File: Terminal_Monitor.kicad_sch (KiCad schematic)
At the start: 10 parts, among them J10 VoltageMonitor, J3 7460553, J4 7460553, J5 7460553, J6 7460553

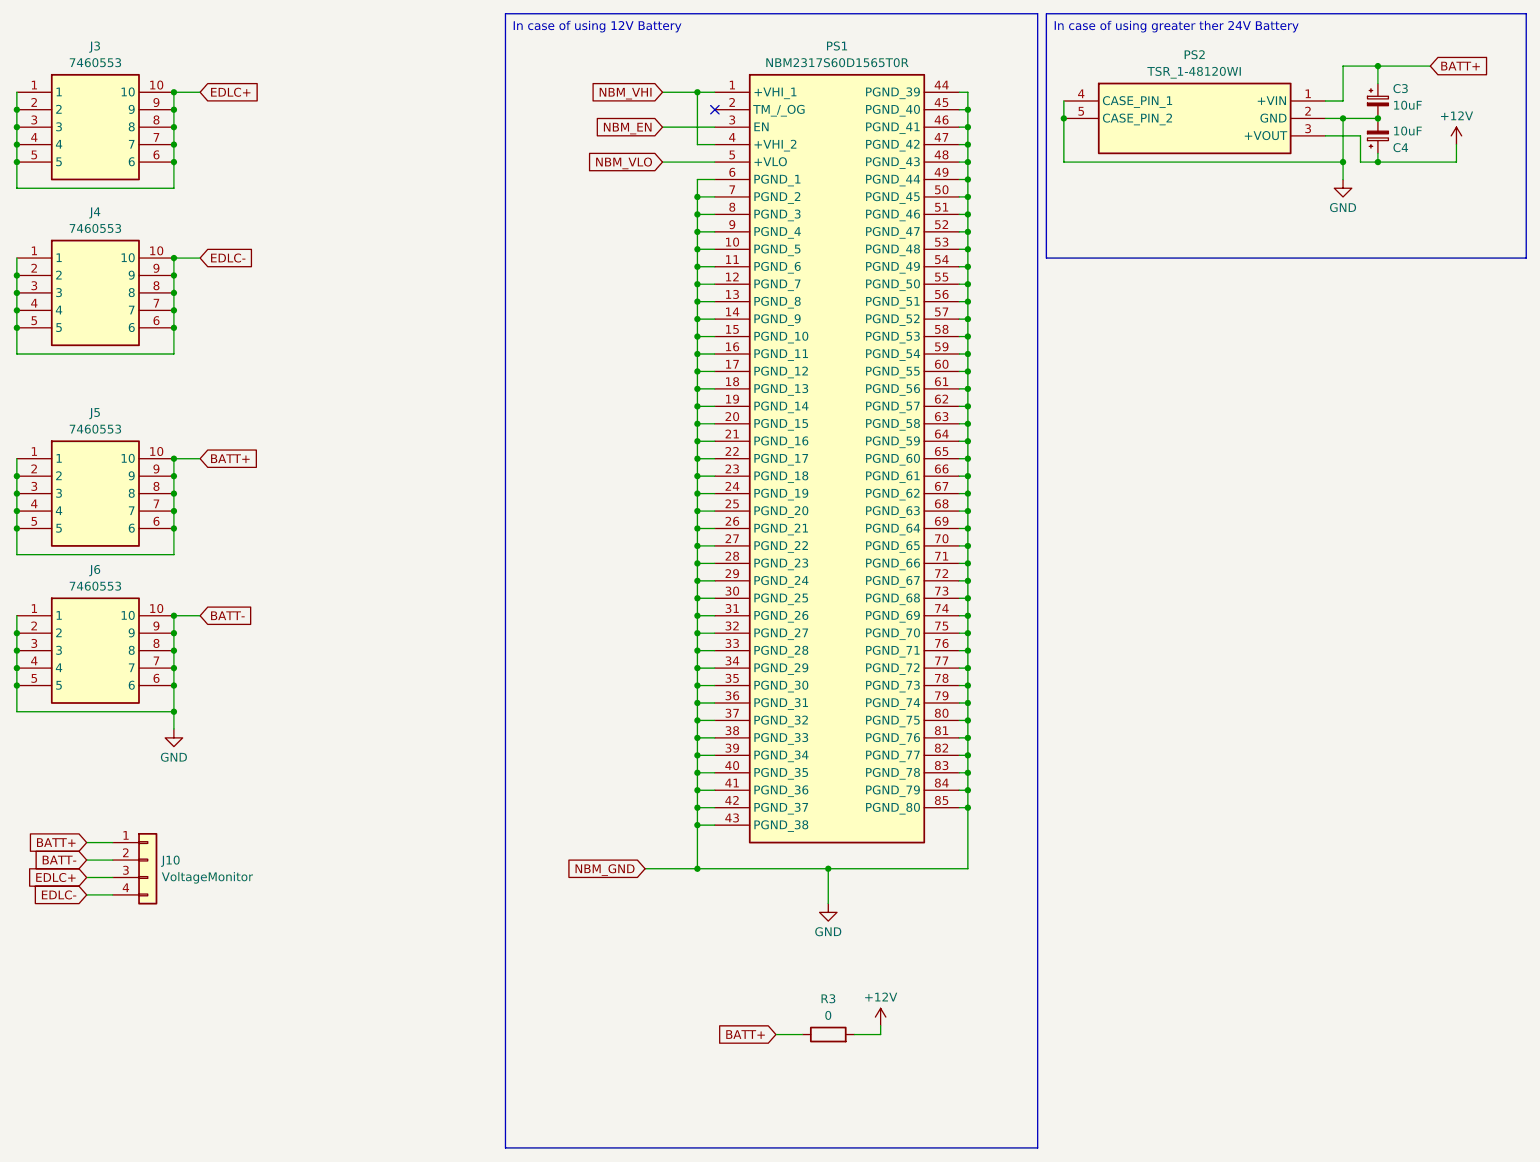
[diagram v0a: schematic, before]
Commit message: Throttle 2pin->3pin and Add C beside of NBM.
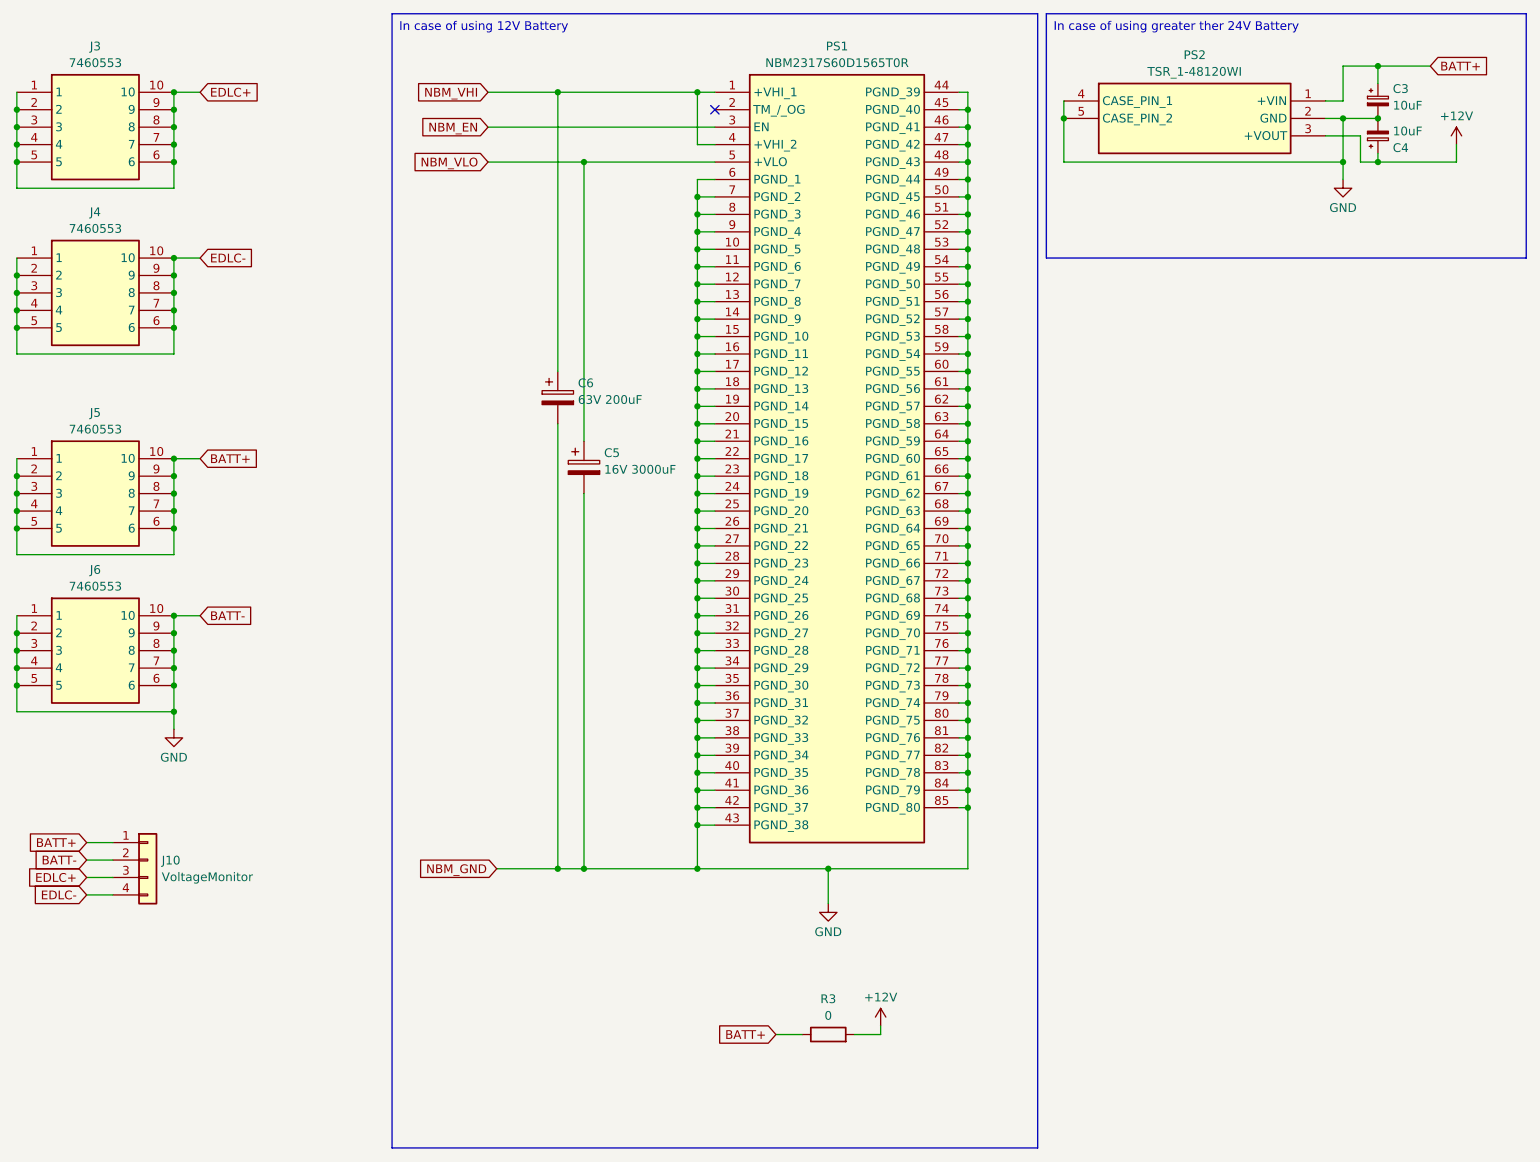
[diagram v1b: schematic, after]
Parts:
- added C5: 16V 3000uF, symbol Device:C_Polarized
- added C6: 63V 200uF, symbol Device:C_Polarized
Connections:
- net GND: now also C5.2, C6.2
- net NBM_VHI: now also C6.1
- net NBM_VLO: now also C5.1

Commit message: layout done
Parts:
- C3, C4: footprint (none) -> Capacitor_THT:CP_Radial_D5.0mm_P2.00mm
- C5: footprint (none) -> Capacitor_THT:CP_Radial_D12.5mm_P5.00mm
- C6: footprint (none) -> Capacitor_THT:CP_Radial_D10.0mm_P5.00mm
- J10: footprint (none) -> Connector_PinHeader_2.54mm:PinHeader_1x04_P2.54mm_Vertical
- J3: value 7460553 -> EDLC+; footprint 7460553 -> 7460553:7460553
- J4: value 7460553 -> EDLC-; footprint 7460553 -> 7460553:7460553
- J5: value 7460553 -> BATT+; footprint 7460553 -> 7460553:7460553
- J6: value 7460553 -> BATT-; footprint 7460553 -> 7460553:7460553
- PS1: footprint NBM2317S60D1565T0R -> NBM2317S60D1565T0R:NBM2317S60D1565T0R
- PS2: footprint TSR148120WI -> TSR_1-48120WI:TSR148120WI
- R3: footprint (none) -> Resistor_THT:R_Axial_DIN0207_L6.3mm_D2.5mm_P2.54mm_Vertical
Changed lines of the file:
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@@
 			)
 		)
-		(property "Footprint" ""
+		(property "Footprint" "Capacitor_THT:CP_Radial_D10.0mm_P5.00mm"
 			(at 105.1052 76.2 0)
 			(effects
@@
 			)
 		)
-		(property "Footprint" "TSR148120WI"
+		(property "Footprint" "TSR_1-48120WI:TSR148120WI"
 			(at 212.09 124.13 0)
 			(effects
@@
 			)
 		)
-		(property "Value" "7460553"
+		(property "Value" "BATT-"
 			(at 36.83 99.8798 0)
 			(effects
@@
 			)
 		)
-		(property "Footprint" "7460553"
+		(property "Footprint" "7460553:7460553"
 			(at 44.45 199.06 0)
 			(effects
@@
 			)
 		)
-		(property "Footprint" ""
+		(property "Footprint" "Resistor_THT:R_Axial_DIN0207_L6.3mm_D2.5mm_P2.54mm_Vertical"
 			(at 143.51 166.878 90)
 			(effects
@@
 			)
 		)
-		(property "Footprint" ""
+		(property "Footprint" "Capacitor_THT:CP_Radial_D5.0mm_P2.00mm"
 			(at 223.52 34.29 0)
 			(effects
@@
 			)
 		)
-		(property "Value" "7460553"
+		(property "Value" "BATT+"
 			(at 36.83 77.0198 0)
 			(effects
@@
 			)
 		)
-		(property "Footprint" "7460553"
+		(property "Footprint" "7460553:7460553"
 			(at 44.45 176.2 0)
 			(effects
@@
 			)
 		)
-		(property "Footprint" ""
+		(property "Footprint" "Capacitor_THT:CP_Radial_D5.0mm_P2.00mm"
 			(at 223.52 29.21 0)
 			(effects
@@
 			)
 		)
-		(property "Footprint" ""
+		(property "Footprint" "Capacitor_THT:CP_Radial_D12.5mm_P5.00mm"
 			(at 108.9152 86.36 0)
 			(effects
@@
 			)
 		)
-		(property "Value" "7460553"
+		(property "Value" "EDLC-"
 			(at 36.83 47.8098 0)
 			(effects
@@
 			)
 		)
-		(property "Footprint" "7460553"
+		(property "Footprint" "7460553:7460553"
 			(at 44.45 146.99 0)
 			(effects
@@
 			)
 		)
-		(property "Value" "7460553"
+		(property "Value" "EDLC+"
 			(at 36.83 23.6798 0)
 			(effects
@@
 			)
 		)
-		(property "Footprint" "7460553"
+		(property "Footprint" "7460553:7460553"
 			(at 44.45 122.86 0)
 			(effects
@@
 			)
 		)
-		(property "Footprint" ""
+		(property "Footprint" "Connector_PinHeader_2.54mm:PinHeader_1x04_P2.54mm_Vertical"
 			(at 44.45 139.7 0)
 			(effects
@@
 			)
 		)
-		(property "Footprint" "NBM2317S60D1565T0R"
+		(property "Footprint" "NBM2317S60D1565T0R:NBM2317S60D1565T0R"
 			(at 158.75 122.86 0)
 			(effects
